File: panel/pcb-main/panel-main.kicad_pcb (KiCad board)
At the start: 2 copper layers, 191.7 x 104.9 mm, 97 parts, among them J1 PSU IN, J2 SPEED CTRL, J3 ICSP, J4 PUSH-BUTTON, J5 DISPLAY, J6 CONN-L1, J7 CONN-L2, J8 CONN-R1, J9 CONN-R2, K1 TRK2233-12DC, K10 TRK2233-12DC, K11 TRK2233-12DC, K2 TRK2233-12DC, K3 TRK2233-12DC, K4 TRK2233-12DC, K5 TRK2233-12DC, K6 TRK2233-12DC, K7 TRK2233-12DC, K8 TRK2233-12DC, K9 TRK2233-12DC, Q1 2N2222, Q10 BD679, Q11 BD679, Q12 BD679, Q13 BD679, Q14 2N2222, Q15 BD679, Q16 BD679, Q17 BD679, Q18 BD679, Q19 BD679, Q2 TIP32, Q3 BD679, Q37 BD679, Q4 BD679, Q5 BD679, Q6 BD679, Q7 BD679, Q8 BD679, Q9 TIP32, U1 LM7805_TO220, U2 74HC595, U3 74HC595, U4 74HC595, U5 74HC595, U6 ULN2003A, U7 ULN2003A, Y1 20MHz

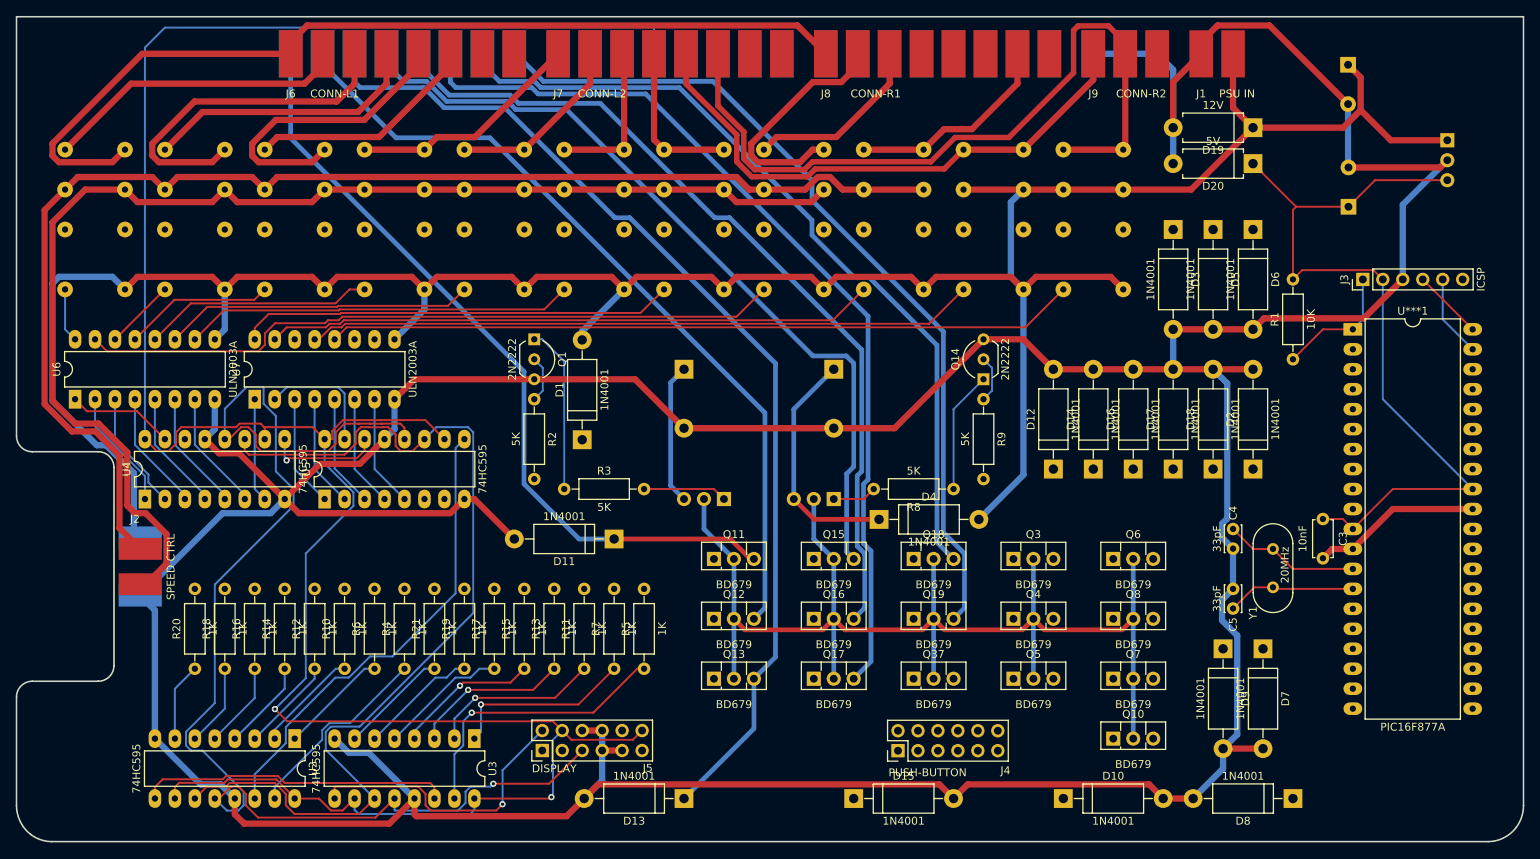
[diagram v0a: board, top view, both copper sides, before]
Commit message: Main PCB Update - MOSFETS on Points, 3 tanks.
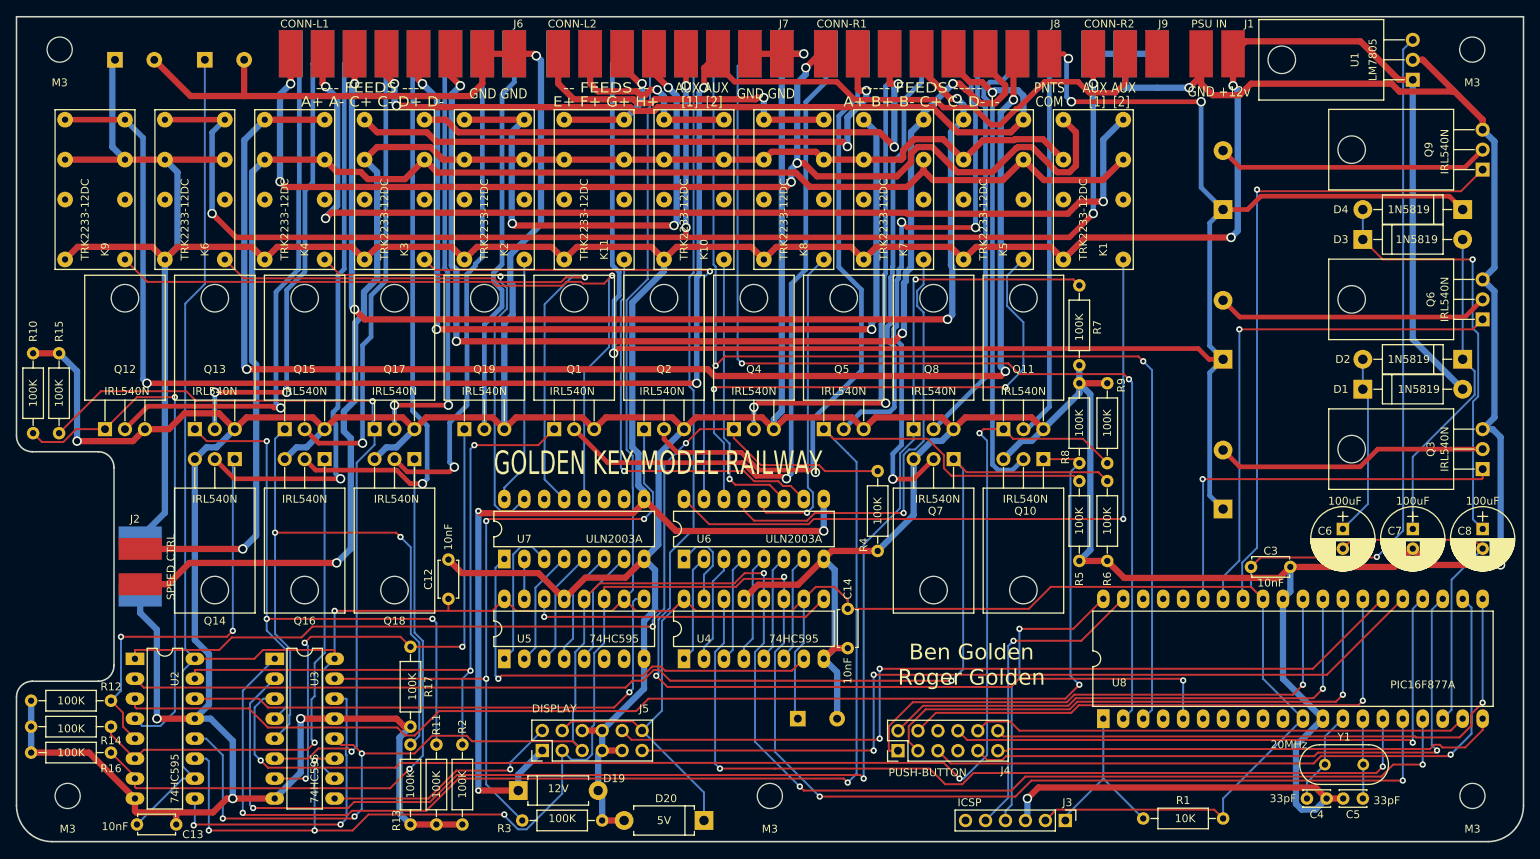
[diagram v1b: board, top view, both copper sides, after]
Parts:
- removed D10, D11, D12, D13, D14, D15, D16, D17, D18, D5, D6, D7, D8, D9: 1N4001, Diodes_THT:D_DO-15_P12.70mm_Horizontal
- removed Q37: BD679, TO_SOT_Packages_THT:TO-126_Vertical
- removed R18, R19, R20, R21: 1K, Resistors_THT:R_Axial_DIN0207_L6.3mm_D2.5mm_P10.16mm_Horizontal
- removed U***1: PIC16F877A, Housings_DIP:DIP-40_W15.24mm_LongPads
- added C10: 4700uF, Capacitors_THT:CP_Radial_D18.0mm_P7.50mm, B.Cu at (204.5, 82.5)
- added C11: 4700uF, Capacitors_THT:CP_Radial_D18.0mm_P7.50mm, B.Cu at (204.5, 63.5)
- added C12: 10nF, Capacitors_THT:C_Disc_D4.7mm_W2.5mm_P5.00mm, F.Cu at (105.9, 113.0)
- added C13: 10nF, Capacitors_THT:C_Disc_D4.7mm_W2.5mm_P5.00mm, F.Cu at (66.3, 141.7)
- added C14: 10nF, Capacitors_THT:C_Disc_D4.7mm_W2.5mm_P5.00mm, F.Cu at (156.7, 114.3)
- added C15: 470uF, Capacitors_THT:CP_Radial_D10.0mm_P5.00mm, B.Cu at (150.4, 128.3)
- added C8: 100uF, Capacitors_THT:CP_Radial_D8.0mm_P2.50mm, F.Cu at (237.5, 104.1)
- added C9: 4700uF, Capacitors_THT:CP_Radial_D18.0mm_P7.50mm, B.Cu at (204.5, 101.6)
- added REF**: M3, Mounting_Holes:MountingHole_3.2mm_M3, F.Cu at (236.2, 43.2)
- added REF**: M3, Mounting_Holes:MountingHole_3.2mm_M3, F.Cu at (56.5, 43.2)
- added REF**: M3, Mounting_Holes:MountingHole_3.2mm_M3, F.Cu at (57.5, 138.1)
- added REF**: M3, Mounting_Holes:MountingHole_3.2mm_M3, F.Cu at (146.8, 138.1)
- added REF**: M3, Mounting_Holes:MountingHole_3.2mm_M3, F.Cu at (236.2, 138.1)
- added U8: PIC16F877A, Housings_DIP:DIP-40_W15.24mm_LongPads, F.Cu at (189.2, 128.3)
- C6, C7: value 4700uF -> 100uF; footprint Capacitors_THT:CP_Radial_D18.0mm_P7.50mm -> Capacitors_THT:CP_Radial_D8.0mm_P2.50mm; moved to F.Cu
- D1, D2, D3, D4: value 1N4001 -> 1N5819
- K1, K10, K11, K2, K3, K4, K5, K6, K7, K8, K9: moved to F.Cu
- Q1, Q14: value 2N2222 -> IRL540N; footprint TO_SOT_Packages_THT:TO-92_Inline_Wide -> TO_SOT_Packages_THT:TO-220-3_Horizontal
- Q10, Q11, Q12, Q13, Q15, Q16, Q17, Q18, Q19, Q3, Q4, Q5, Q6, Q7, Q8: value BD679 -> IRL540N; footprint TO_SOT_Packages_THT:TO-126_Vertical -> TO_SOT_Packages_THT:TO-220-3_Horizontal
- Q2, Q9: value TIP32 -> IRL540N; footprint TO_SOT_Packages_THT:TO-220-3_Vertical -> TO_SOT_Packages_THT:TO-220-3_Horizontal; moved to F.Cu
- R10, R11, R12, R13, R14, R15, R16, R17, R4, R5, R6, R7: value 1K -> 100K
- R2, R3, R8, R9: value 5K -> 100K
- U1: value LM7805_TO220 -> LM7805; footprint TO_SOT_Packages_THT:TO-220-3_Vertical -> TO_SOT_Packages_THT:TO-220-3_Horizontal; moved to F.Cu
- moved C1 156.9 mm to (63.5, 44.5), turned to 0 degrees
- moved C2 146.7 mm to (74.9, 44.5), turned to 0 degrees
- moved K9 134.7 mm to (57.1, 69.8)
- moved D19 125.9 mm to (114.8, 137.4), turned to 0 degrees
- moved K1 119.4 mm to (184.2, 69.8)
- moved K6 109.3 mm to (69.8, 69.8)
- moved D20 108.9 mm to (138.4, 141.2)
- moved D1 99.5 mm to (222.2, 86.4), turned to 0 degrees
- moved R6 96.2 mm to (189.7, 98.0), turned to 270 degrees
- moved Q14 95.8 mm to (78.7, 95.2), turned to 180 degrees
- moved K5 94.1 mm to (171.4, 69.8)
- moved Q9 92.6 mm to (237.5, 58.4), turned to 90 degrees
- moved C6 86.2 mm to (219.7, 104.1)
- moved D4 84.1 mm to (234.9, 63.5), turned to 180 degrees
- moved K4 83.9 mm to (82.5, 69.8)
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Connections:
- C6 pad 1: /Points Control/TANKCAP1 -> Net-(C6-Pad1)
- C6 pad 2: GND -> /Points Control/CHARGE-PUMP
- C7 pad 1: /Points Control/TANKCAP2 -> Net-(C7-Pad1)
- D1 pad 1: /Points Control/TANKCAP1 -> Net-(C6-Pad1)
- D2 pad 1: /Points Control/POINTS[B1]-COIL -> Net-(C7-Pad1)
- D2 pad 2: GND -> Net-(C6-Pad1)
- D3 pad 1: /Points Control/POINTS[F1]-COIL -> Net-(C8-Pad1)
- D3 pad 2: GND -> Net-(C7-Pad1)
- D4 pad 1: /Points Control/TANKCAP2 -> /Points Control/POINTS[COM]
- D4 pad 2: +12V -> Net-(C8-Pad1)
- J7 pad 14: Net-(J7-Pad14) -> /Points Control/POINTS[COM]
- J8 pad 8: Net-(J8-Pad8) -> /Points Control/POINTS[COM]
- Q1 pad 1: Net-(Q1-Pad1) -> /Points Control/PB1
- Q1 pad 2: Net-(Q1-Pad2) -> /Points Control/POINTS[B1]-COIL
- Q10 pad 1: Net-(Q10-Pad1) -> /Points Control/PB4
- Q10 pad 2: TANK-DUMP -> /Points Control/POINTS[B4]-COIL
- Q10 pad 3: /Points Control/POINTS[F4]-COIL -> GND
- Q11 pad 1: Net-(Q11-Pad1) -> /Points Control/PF4
- Q11 pad 2: TANK-DUMP -> /Points Control/POINTS[F4]-COIL
- Q11 pad 3: /Points Control/POINTS[B5]-COIL -> GND
- Q12 pad 1: Net-(Q12-Pad1) -> /Points Control/PB5
- Q12 pad 2: TANK-DUMP -> /Points Control/POINTS[B5]-COIL
- Q12 pad 3: /Points Control/POINTS[F5]-COIL -> GND
- Q13 pad 1: Net-(Q13-Pad1) -> /Points Control/PF5
- Q13 pad 2: TANK-DUMP -> /Points Control/POINTS[F5]-COIL
- Q13 pad 3: /Points Control/POINTS[B6]-COIL -> GND
- Q14 pad 1: Net-(Q14-Pad1) -> /Points Control/PB6
- Q14 pad 2: Net-(Q14-Pad2) -> /Points Control/POINTS[B6]-COIL
- Q15 pad 1: Net-(Q15-Pad1) -> /Points Control/PF6
- Q15 pad 2: TANK-DUMP -> /Points Control/POINTS[F6]-COIL
- Q15 pad 3: /Points Control/POINTS[F6]-COIL -> GND
- Q16 pad 1: Net-(Q16-Pad1) -> /Points Control/PB7
- Q16 pad 2: TANK-DUMP -> /Points Control/POINTS[B7]-COIL
- Q16 pad 3: /Points Control/POINTS[B7]-COIL -> GND
- Q17 pad 1: Net-(Q17-Pad1) -> /Points Control/PF7
- Q17 pad 2: TANK-DUMP -> /Points Control/POINTS[F7]-COIL
- Q17 pad 3: /Points Control/POINTS[F7]-COIL -> GND
- Q18 pad 1: Net-(Q18-Pad1) -> /Points Control/PB8
- Q18 pad 2: TANK-DUMP -> /Points Control/POINTS[B8]-COIL
- Q18 pad 3: /Points Control/POINTS[B8]-COIL -> GND
- Q19 pad 1: Net-(Q19-Pad1) -> /Points Control/PF8
- Q19 pad 2: TANK-DUMP -> /Points Control/POINTS[F8]-COIL
- Q19 pad 3: /Points Control/POINTS[F8]-COIL -> GND
- Q2 pad 1: Net-(Q2-Pad1) -> /Points Control/PF1
- Q2 pad 2: TANK-DUMP -> /Points Control/POINTS[F1]-COIL
- Q2 pad 3: /Points Control/TANKCAP1 -> GND
- Q3 pad 1: Net-(Q3-Pad1) -> /Points Control/TANK-1
- Q3 pad 2: TANK-DUMP -> /Points Control/TANK-1-GND
- Q3 pad 3: /Points Control/POINTS[F1]-COIL -> GND
- Q4 pad 1: Net-(Q4-Pad1) -> /Points Control/PB2
- Q4 pad 2: TANK-DUMP -> /Points Control/POINTS[B2]-COIL
- Q4 pad 3: /Points Control/POINTS[B2]-COIL -> GND
- Q5 pad 1: Net-(Q5-Pad1) -> /Points Control/PF2
- Q5 pad 2: TANK-DUMP -> /Points Control/POINTS[F2]-COIL
- Q5 pad 3: /Points Control/POINTS[F2]-COIL -> GND
- Q6 pad 1: Net-(Q6-Pad1) -> /Points Control/TANK-2
- Q6 pad 2: TANK-DUMP -> /Points Control/TANK-2-GND
- Q6 pad 3: /Points Control/POINTS[B3]-COIL -> GND
- Q7 pad 1: Net-(Q7-Pad1) -> /Points Control/PB3
- Q7 pad 2: TANK-DUMP -> /Points Control/POINTS[B3]-COIL
- Q7 pad 3: /Points Control/POINTS[F3]-COIL -> GND
- Q8 pad 1: Net-(Q8-Pad1) -> /Points Control/PF3
- Q8 pad 2: TANK-DUMP -> /Points Control/POINTS[F3]-COIL
- Q8 pad 3: /Points Control/POINTS[B4]-COIL -> GND
- Q9 pad 1: Net-(Q9-Pad1) -> /Points Control/TANK-3
- Q9 pad 2: TANK-DUMP -> /Points Control/TANK-3-GND
- Q9 pad 3: /Points Control/TANKCAP2 -> GND
- R10 pad 1: /Points Control/PB3 -> /Points Control/PB5
- R10 pad 2: Net-(Q6-Pad1) -> GND
- R11 pad 1: /Points Control/PF3 -> /Points Control/PF5
- R11 pad 2: Net-(Q7-Pad1) -> GND
- R12 pad 1: /Points Control/PB4 -> /Points Control/PB6
- R12 pad 2: Net-(Q8-Pad1) -> GND
- R13 pad 1: /Points Control/PF4 -> /Points Control/PF6
- R13 pad 2: Net-(Q10-Pad1) -> GND
- R14 pad 1: /Points Control/PB5 -> /Points Control/PB7
- R14 pad 2: Net-(Q11-Pad1) -> GND
- R15 pad 1: /Points Control/PF5 -> /Points Control/PF7
- R15 pad 2: Net-(Q12-Pad1) -> GND
- R16 pad 1: /Points Control/PB6 -> /Points Control/PB8
- R16 pad 2: Net-(Q13-Pad1) -> GND
- R17 pad 1: /Points Control/PF6 -> /Points Control/PF8
- R17 pad 2: Net-(Q15-Pad1) -> GND
- R2 pad 1: Net-(Q1-Pad2) -> /Points Control/PB1
- R2 pad 2: /Points Control/TANK[1] -> GND
- R3 pad 1: Net-(Q1-Pad1) -> /Points Control/PF1
- R3 pad 2: Net-(Q2-Pad1) -> GND
- R4 pad 1: /Points Control/PB1 -> /Points Control/PB2
- R4 pad 2: Net-(Q37-Pad1) -> GND
- R5 pad 1: /Points Control/PF1 -> /Points Control/PF2
- R5 pad 2: Net-(Q3-Pad1) -> GND
- R6 pad 1: /Points Control/PB2 -> /Points Control/PB3
- R6 pad 2: Net-(Q4-Pad1) -> GND
- R7 pad 1: /Points Control/PF2 -> /Points Control/PF3
- R7 pad 2: Net-(Q5-Pad1) -> GND
- R8 pad 1: Net-(Q14-Pad1) -> /Points Control/PB4
- R8 pad 2: Net-(Q9-Pad1) -> GND
- R9 pad 1: Net-(Q14-Pad2) -> /Points Control/PF4
- R9 pad 2: /Points Control/TANK[2] -> GND
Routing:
- net GND: track 628.9 -> 977.3 mm, vias 0 -> 9
- net /Points Control/POINTS[COM]: track 0.00 -> 230.3 mm, vias 0 -> 4
- net /Points Control/PF3: track 21.7 -> 184.9 mm, vias 1 -> 3
- net /Points Control/PF2: track 23.5 -> 183.9 mm, vias 1 -> 2
- net TANK-DUMP: track 157.1 -> 0.00 mm
- net /HALL[E]: track 0.00 -> 154.9 mm, vias 0 -> 2
- net /Feed Relays/FEED[I-]: track 26.8 -> 179.2 mm, vias 0 -> 3
- net /Points Control/PB4: track 12.0 -> 159.3 mm, vias 0 -> 1
- net /Points Control/PF4: track 20.0 -> 164.8 mm, vias 1 -> 3
- net /Points Control/PB3: track 13.2 -> 155.9 mm, vias 0 -> 1
- net /HALL[F]: track 0.00 -> 141.6 mm, vias 0 -> 2
- net /HALL[G]: track 0.00 -> 134.1 mm, vias 0 -> 2
- net +5V: track 421.5 -> 553.3 mm
- net +12V: track 341.4 -> 469.3 mm, vias 0 -> 5
- net /Feed Relays/AUX[2]: track 96.8 -> 218.7 mm, vias 0 -> 3
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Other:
- net class Aux Feeds: via_dia 0.8 -> 1.2; via_drill 0.4 -> 0.8
- net class Points Coils: via_dia 0.8 -> 1.2; via_drill 0.4 -> 0.8
- net class Power: via_dia 0.8 -> 1.2; via_drill 0.4 -> 0.8
- net class Track Feeds: via_dia 1 -> 1.2
- board text added: "+5v"
- board text added: "-- FEEDS --"
- board text added: "---- FEEDS ----"
- board text added: "----- FEEDS -----"
- board text added: "------ POINTS ------"
- board text added: "A+ A- C+ C- D+ D-"
- board text added: "A+ B+ B- C+ C- D- I-"
- board text added: "AUX AUX"
- board text added: "Ben Golden Roger Golden"
- board text added: "COM"
- board text added: "E+ F+ G+ H+"
- board text added: "F4 B4 F3 B3 F2 B2 F1 B1"
- board text added: "F8 B8 F7 B7 F6 B6 F5 B5"
- board text added: "GND"
- board text added: "GND +12v"
- board text added: "GND GND"
- board text added: "GND GND GND"
- board text added: "GOLDEN KEY MODEL RAILWAY"
- board text added: "HALL SENSORS"
- board text added: "PNTS"
- board text added: "[1] [2]"
- board text added: "[G] [F] [E]"

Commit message: Completed all PCBs and added gerber files
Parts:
- removed C10, C11: 4700uF, Capacitors_THT:CP_Radial_D18.0mm_P7.50mm
- added D5: RUNNING, LEDs:LED_D5.0mm, F.Cu at (206.2, 106.2)
- added D6: CHARGING, LEDs:LED_D5.0mm, F.Cu at (200.2, 106.2)
- added D7: SWITCHING, LEDs:LED_D5.0mm, F.Cu at (194.1, 106.2)
- added J11: REVERSE, Pin_Headers:Pin_Header_Straight_2x03_Pitch2.54mm, B.Cu at (66.4, 100.7)
- added R18: 47K, Resistors_THT:R_Axial_DIN0207_L6.3mm_D2.5mm_P10.16mm_Horizontal, F.Cu at (223.5, 97.5)
- added R19: 10K, Resistors_THT:R_Axial_DIN0207_L6.3mm_D2.5mm_P10.16mm_Horizontal, F.Cu at (220.6, 107.7)
- added R20: 2.2K, Resistors_THT:R_Axial_DIN0207_L6.3mm_D2.5mm_P10.16mm_Horizontal, F.Cu at (229.4, 97.5)
- added R21: 4.7K, Resistors_THT:R_Axial_DIN0207_L6.3mm_D2.5mm_P10.16mm_Horizontal, F.Cu at (110.2, 95.0)
- added R22: 4.7K, Resistors_THT:R_Axial_DIN0207_L6.3mm_D2.5mm_P10.16mm_Horizontal, F.Cu at (111.0, 131.6)
- added R23: 100K, Resistors_THT:R_Axial_DIN0207_L6.3mm_D2.5mm_P10.16mm_Horizontal, F.Cu at (226.4, 97.5)
- added R24: 4.7K, Resistors_THT:R_Axial_DIN0207_L6.3mm_D2.5mm_P10.16mm_Horizontal, F.Cu at (158.0, 106.9)
- added R25: 4.7K, Resistors_THT:R_Axial_DIN0207_L6.3mm_D2.5mm_P10.16mm_Horizontal, F.Cu at (192.8, 102.9)
- added R26: 4.7K, Resistors_THT:R_Axial_DIN0207_L6.3mm_D2.5mm_P10.16mm_Horizontal, F.Cu at (195.6, 102.9)
- added R27: 4.7K, Resistors_THT:R_Axial_DIN0207_L6.3mm_D2.5mm_P10.16mm_Horizontal, F.Cu at (189.0, 83.3)
- added R28: 4.7K, Resistors_THT:R_Axial_DIN0207_L6.3mm_D2.5mm_P10.16mm_Horizontal, F.Cu at (195.6, 80.3)
- added R29: 4.7K, Resistors_THT:R_Axial_DIN0207_L6.3mm_D2.5mm_P10.16mm_Horizontal, F.Cu at (192.8, 80.3)
- added R30: 4.7K, Resistors_THT:R_Axial_DIN0207_L6.3mm_D2.5mm_P10.16mm_Horizontal, F.Cu at (53.3, 62.5)
- added R31: 4.7K, Resistors_THT:R_Axial_DIN0207_L6.3mm_D2.5mm_P10.16mm_Horizontal, F.Cu at (106.2, 119.1)
- added R32: 4.7K, Resistors_THT:R_Axial_DIN0207_L6.3mm_D2.5mm_P10.16mm_Horizontal, F.Cu at (75.7, 116.8)
- added R33: 4.7K, Resistors_THT:R_Axial_DIN0207_L6.3mm_D2.5mm_P10.16mm_Horizontal, F.Cu at (97.8, 141.7)
- added R34: 4.7K, Resistors_THT:R_Axial_DIN0207_L6.3mm_D2.5mm_P10.16mm_Horizontal, F.Cu at (78.5, 117.6)
- added R35: 4.7K, Resistors_THT:R_Axial_DIN0207_L6.3mm_D2.5mm_P10.16mm_Horizontal, F.Cu at (53.3, 65.5)
- added R36: 4.7K, Resistors_THT:R_Axial_DIN0207_L6.3mm_D2.5mm_P10.16mm_Horizontal, F.Cu at (63.0, 133.1)
- added R37: 4.7K, Resistors_THT:R_Axial_DIN0207_L6.3mm_D2.5mm_P10.16mm_Horizontal, F.Cu at (98.3, 129.3)
- added R38: 240, Resistors_THT:R_Axial_DIN0207_L6.3mm_D2.5mm_P10.16mm_Horizontal, F.Cu at (217.7, 107.7)
- added R39: 240, Resistors_THT:R_Axial_DIN0207_L6.3mm_D2.5mm_P10.16mm_Horizontal, F.Cu at (214.8, 107.7)
- added R40: 240, Resistors_THT:R_Axial_DIN0207_L6.3mm_D2.5mm_P10.16mm_Horizontal, F.Cu at (211.8, 107.7)
- added R41: 4.7K, Resistors_THT:R_Axial_DIN0207_L6.3mm_D2.5mm_P10.16mm_Horizontal, F.Cu at (232.3, 97.5)
- J3: moved to B.Cu
- Q3: value IRL540N -> 2N2219; footprint TO_SOT_Packages_THT:TO-220-3_Horizontal -> TO_SOT_Packages_THT:TO-92_Inline_Wide
- moved C8 40.9 mm to (208.4, 75.4), turned to 90 degrees
- moved C9 38.7 mm to (201.9, 63.0)
- moved C6 35.1 mm to (199.5, 75.4), turned to 90 degrees
- moved D2 31.2 mm to (203.8, 80.6), turned to 270 degrees
- moved C7 30.8 mm to (217.2, 75.6), turned to 90 degrees
- moved Q3 29.8 mm to (228.2, 68.2), turned to 270 degrees
- moved D4 28.3 mm to (212.5, 80.6), turned to 270 degrees
- moved D1 23.4 mm to (199.5, 80.6), turned to 270 degrees
- moved D3 19.4 mm to (208.2, 80.6), turned to 270 degrees
- moved Q9 10.9 mm to (233.7, 68.6), turned to 0 degrees
- moved Q6 5.24 mm to (238.8, 72.4), turned to 180 degrees
- moved R16 2.03 mm to (63.0, 130.6)
- moved C3 1.98 mm to (209.6, 110.2)
- moved J3 1.35 mm to (185.3, 140.2), turned to 90 degrees
- moved R14 1.27 mm to (63.0, 128.0)
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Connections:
- C6 pad 2: /Points Control/CHARGE-PUMP -> Net-(C6-Pad2)
- C8 pad 2: /Points Control/CHARGE-PUMP -> Net-(C6-Pad2)
- C9 pad 2: /Points Control/TANK-1-GND -> GND
- J2 pad 2: TRACK- -> /TFEED[-]
- J2 pad 3: TRACK+ -> /TFEED[+]
- Q1 pad 1: /Points Control/PB1 -> Net-(Q1-Pad1)
- Q10 pad 1: /Points Control/PB4 -> Net-(Q10-Pad1)
- Q11 pad 1: /Points Control/PF4 -> Net-(Q11-Pad1)
- Q12 pad 1: /Points Control/PB5 -> Net-(Q12-Pad1)
- Q13 pad 1: /Points Control/PF5 -> Net-(Q13-Pad1)
- Q14 pad 1: /Points Control/PB6 -> Net-(Q14-Pad1)
- Q15 pad 1: /Points Control/PF6 -> Net-(Q15-Pad1)
- Q16 pad 1: /Points Control/PB7 -> Net-(Q16-Pad1)
- Q17 pad 1: /Points Control/PF7 -> Net-(Q17-Pad1)
- Q18 pad 1: /Points Control/PB8 -> Net-(Q18-Pad1)
- Q19 pad 1: /Points Control/PF8 -> Net-(Q19-Pad1)
- Q2 pad 1: /Points Control/PF1 -> Net-(Q2-Pad1)
- Q3 pad 1: /Points Control/TANK-1 -> GND
- Q3 pad 2: /Points Control/TANK-1-GND -> Net-(Q3-Pad2)
- Q3 pad 3: GND -> Net-(Q3-Pad3)
- Q4 pad 1: /Points Control/PB2 -> Net-(Q4-Pad1)
- Q5 pad 1: /Points Control/PF2 -> Net-(Q5-Pad1)
- Q6 pad 1: /Points Control/TANK-2 -> Net-(Q3-Pad3)
- Q6 pad 2: /Points Control/TANK-2-GND -> +12V
- Q6 pad 3: GND -> Net-(C6-Pad2)
- Q7 pad 1: /Points Control/PB3 -> Net-(Q7-Pad1)
- Q8 pad 1: /Points Control/PF3 -> Net-(Q8-Pad1)
- Q9 pad 1: /Points Control/TANK-3 -> Net-(Q9-Pad1)
- Q9 pad 2: /Points Control/TANK-3-GND -> Net-(C6-Pad2)
- R10 pad 1: /Points Control/PB5 -> Net-(Q12-Pad1)
- R11 pad 1: /Points Control/PF5 -> Net-(Q13-Pad1)
- R12 pad 1: /Points Control/PB6 -> Net-(Q14-Pad1)
- R13 pad 1: /Points Control/PF6 -> Net-(Q15-Pad1)
- R14 pad 1: /Points Control/PB7 -> Net-(Q16-Pad1)
- R15 pad 1: /Points Control/PF7 -> Net-(Q17-Pad1)
- R16 pad 1: /Points Control/PB8 -> Net-(Q18-Pad1)
- R17 pad 1: /Points Control/PF8 -> Net-(Q19-Pad1)
- R2 pad 1: /Points Control/PB1 -> Net-(Q1-Pad1)
- R3 pad 1: /Points Control/PF1 -> Net-(Q2-Pad1)
- R4 pad 1: /Points Control/PB2 -> Net-(Q4-Pad1)
- R5 pad 1: /Points Control/PF2 -> Net-(Q5-Pad1)
- R6 pad 1: /Points Control/PB3 -> Net-(Q7-Pad1)
- R7 pad 1: /Points Control/PF3 -> Net-(Q8-Pad1)
- R8 pad 1: /Points Control/PB4 -> Net-(Q10-Pad1)
- R9 pad 1: /Points Control/PF4 -> Net-(Q11-Pad1)
- U8 pad 33: /Points Control/TANK-3 -> Net-(U8-Pad33)
- U8 pad 34: /Points Control/TANK-2 -> Net-(U8-Pad34)
- U8 pad 35: /Points Control/TANK-1 -> Net-(U8-Pad35)
- U8 pad 4: Net-(U8-Pad4) -> /HALL[E]
- U8 pad 5: /HALL[E] -> /CHG-LVL
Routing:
- net Net-(Q18-Pad1): track 0.00 -> 96.9 mm, vias 0 -> 1
- net /Points Control/TANK-3: track 82.8 -> 0.00 mm, vias 1 -> 0
- net /Points Control/PB8: track 82.2 -> 4.21 mm, vias 1 -> 0
- net Net-(Q2-Pad1): track 0.00 -> 75.7 mm, vias 0 -> 2
- net Net-(Q13-Pad1): track 0.00 -> 74.8 mm, vias 0 -> 2
- net /Points Control/TANK-2: track 66.6 -> 0.00 mm, vias 1 -> 0
- net /Points Control/PF1: track 91.8 -> 27.4 mm, vias 3 -> 1
- net Net-(Q17-Pad1): track 0.00 -> 63.5 mm, vias 0 -> 1
- net /Points Control/PF6: track 85.6 -> 23.6 mm, vias 2 -> 1
- net Net-(Q16-Pad1): track 0.00 -> 57.9 mm, vias 0 -> 1
- net /Points Control/PF2: track 183.9 -> 126.3 mm, vias 2 -> 1
- net Net-(Q15-Pad1): track 0.00 -> 56.8 mm, vias 0 -> 1
- net /CHG-LVL: track 0.00 -> 53.7 mm, vias 0 -> 2
- net /Points Control/PF5: track 84.1 -> 30.5 mm, vias 3 -> 1
- net /Points Control/TANK-1: track 52.1 -> 0.00 mm, vias 1 -> 0
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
